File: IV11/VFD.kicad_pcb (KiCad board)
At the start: 2 copper layers, 225 x 80 mm, 72 parts, among them J1 USB_B, SW1 switch, SW2 switch, SW3 switch, SW4 switch, U1 74HC595, U10 UDN2981, U11 UDN2981, U12 UDN2981, U13 WeMos_mini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

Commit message: Remove OSHW logo - unfortunately with the generic modules, we can't meet OSHW requirements
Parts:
- removed the REF** at (55.4, 26.3)

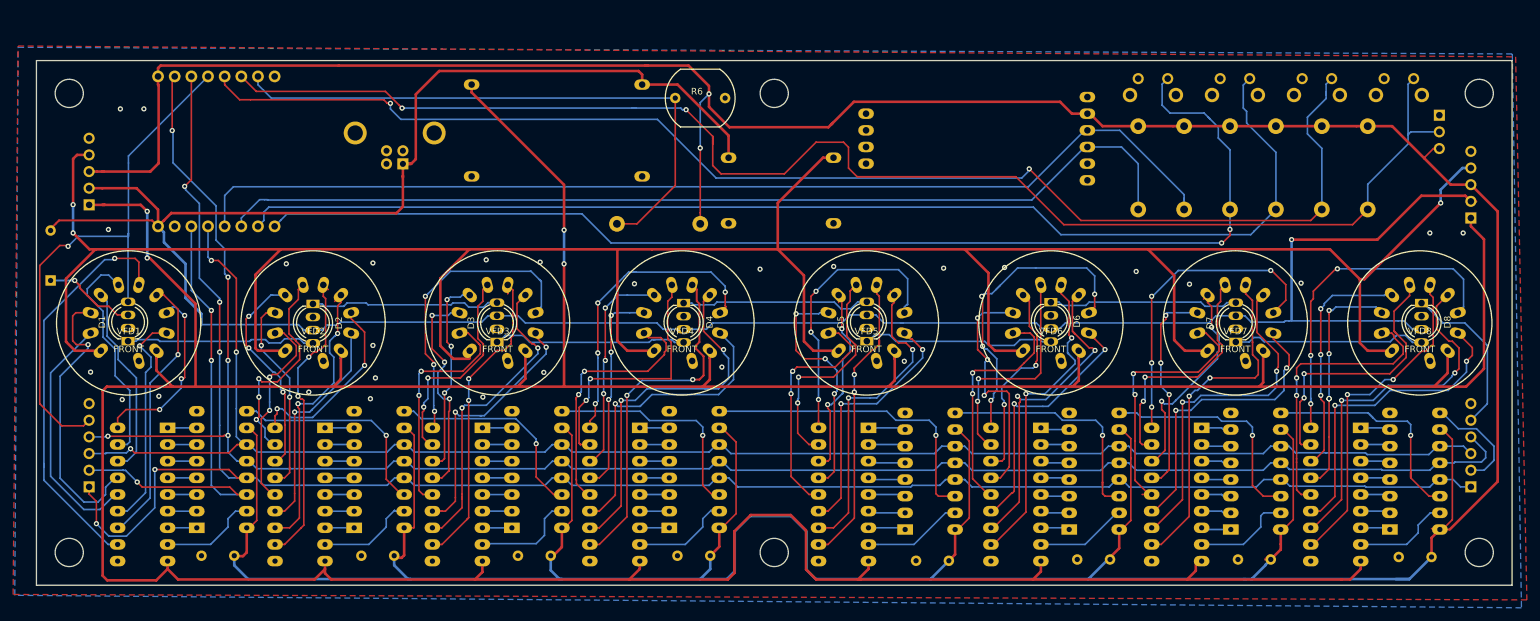
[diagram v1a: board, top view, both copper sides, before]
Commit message: Final updates to complete PCB revision 1.2 including an I2C breakout connector
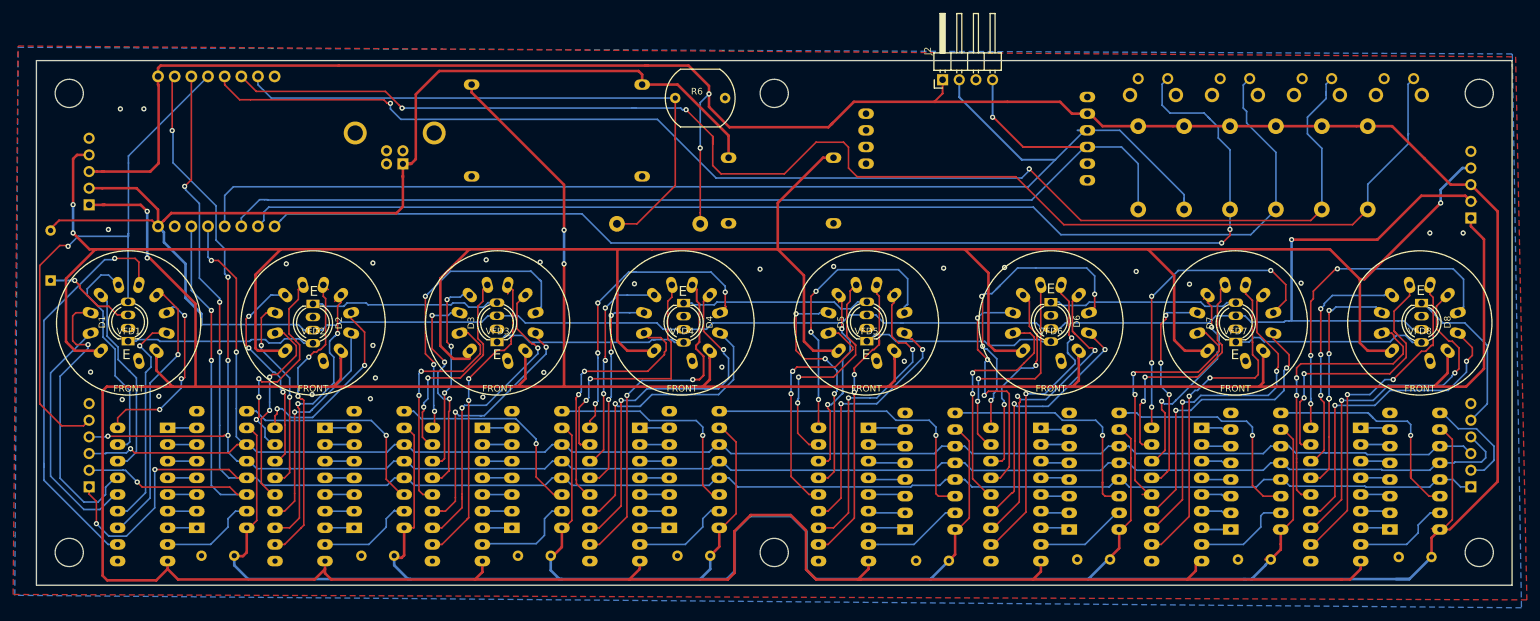
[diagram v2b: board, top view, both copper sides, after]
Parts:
- removed DS18B20: DS18B20, Connector_PinHeader_2.54mm:PinHeader_1x03_P2.54mm_Vertical
- added J2: I2C_CONN, Connector_PinHeader_2.54mm:PinHeader_1x04_P2.54mm_Horizontal, F.Cu at (138.2, 2.92)
- R5: value 100k -> 22k
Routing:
- net SCL: track 150.6 -> 174.2 mm, vias 0 -> 1
- net SDA: track 161.3 -> 184.1 mm
- net SW_1: track 220.2 -> 215.4 mm
- net +3V3: track 733.6 -> 735.1 mm
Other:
- board text added: "E"

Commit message: Major redesign to use different buck converter, and also up-rate track thickness for power rails
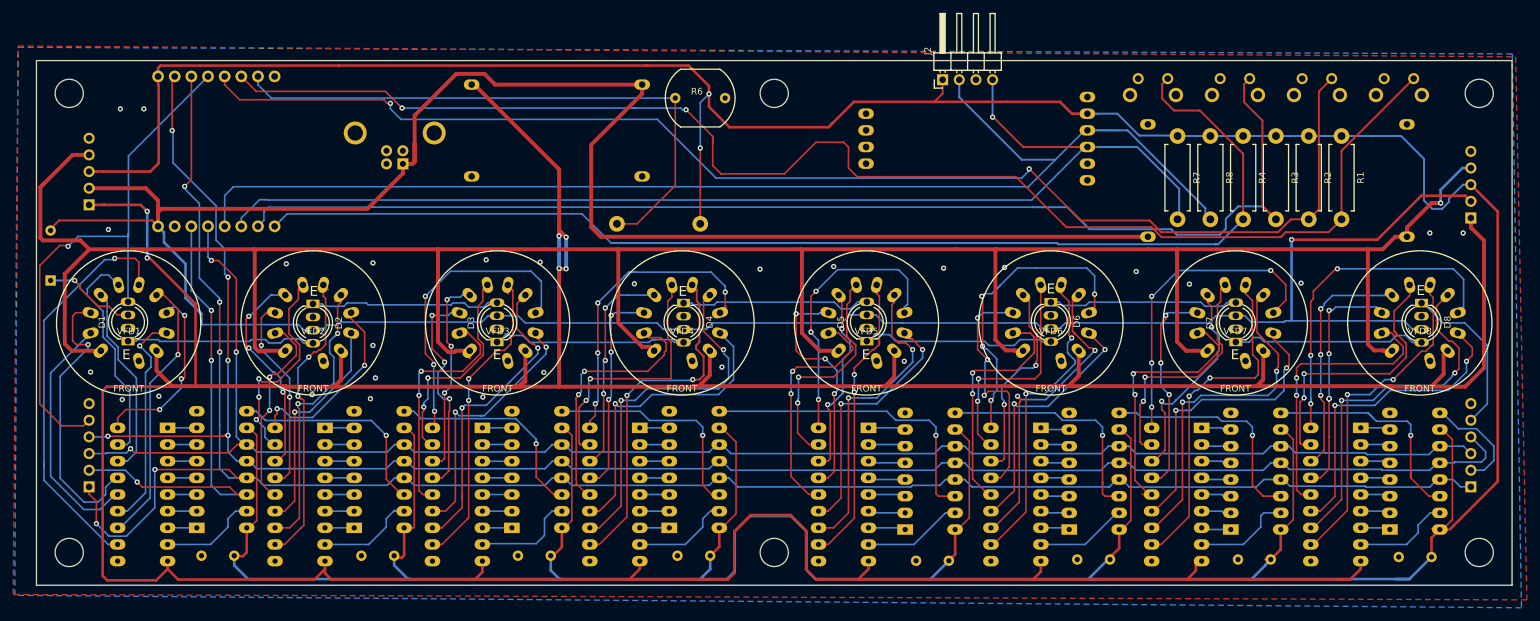
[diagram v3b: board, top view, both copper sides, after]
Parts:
- R1, R2, R3, R4, R7, R8: moved to F.Cu
- U18: value MiniBuckBoard -> LM2596BuckConverterModule; footprint GenericModules:MP2307BuckConverterModule -> GenericModules:LM2596BuckConverterModule
- moved U18 75.7 mm to (189.2, 18.3), turned to 0 degrees
- moved R7 6.18 mm to (174.0, 11.5)
- moved R1 4.27 mm to (199.0, 11.5)
- moved R8 4.27 mm to (179.0, 11.5)
- moved R2 2.50 mm to (194.0, 11.5)
- moved R4 2.50 mm to (184.0, 11.5)
- moved R3 1.50 mm to (189.0, 11.5)
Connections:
- U18 pad 1: +1V5 -> +5V
- U18 pad 4: +5V -> +1V5
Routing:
- net +36V: track 637.5 -> 748.7 mm, vias 4 -> 6
- net +5V: track 402.5 -> 488.4 mm
- net +1V5: track 422.7 -> 403.2 mm, vias 3 -> 1
- net SCL: track 174.2 -> 183.2 mm
- net +3V3: track 735.1 -> 741.9 mm
- net SDA: track 184.1 -> 190.7 mm
- net SW_3: track 182.9 -> 186.3 mm
- net SW_4: track 180.8 -> 181.4 mm, vias 2 -> 0
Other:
- board text added: "V1.3"
- board text removed: "1"
- board text removed: "2"
- board text removed: "3"
- board text removed: "V1.2"

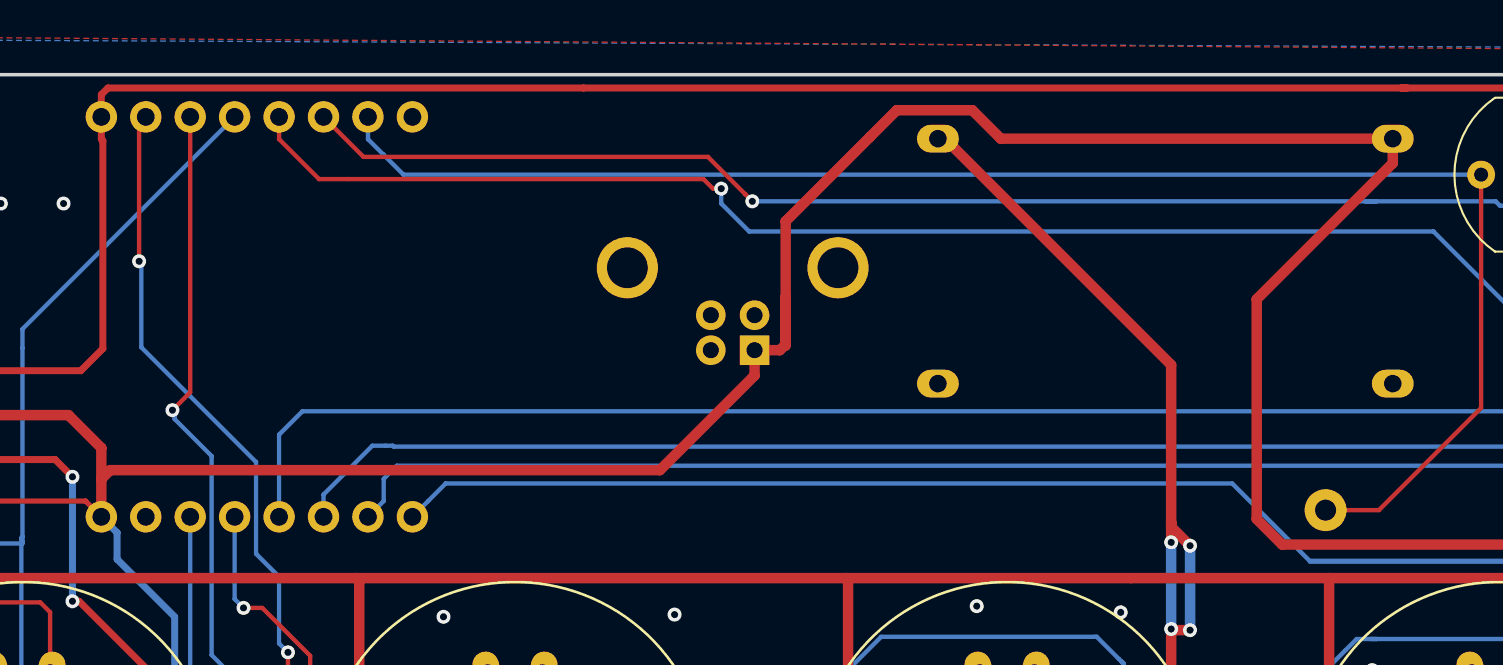
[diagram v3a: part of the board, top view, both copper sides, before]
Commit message: Add in room for polyfuse
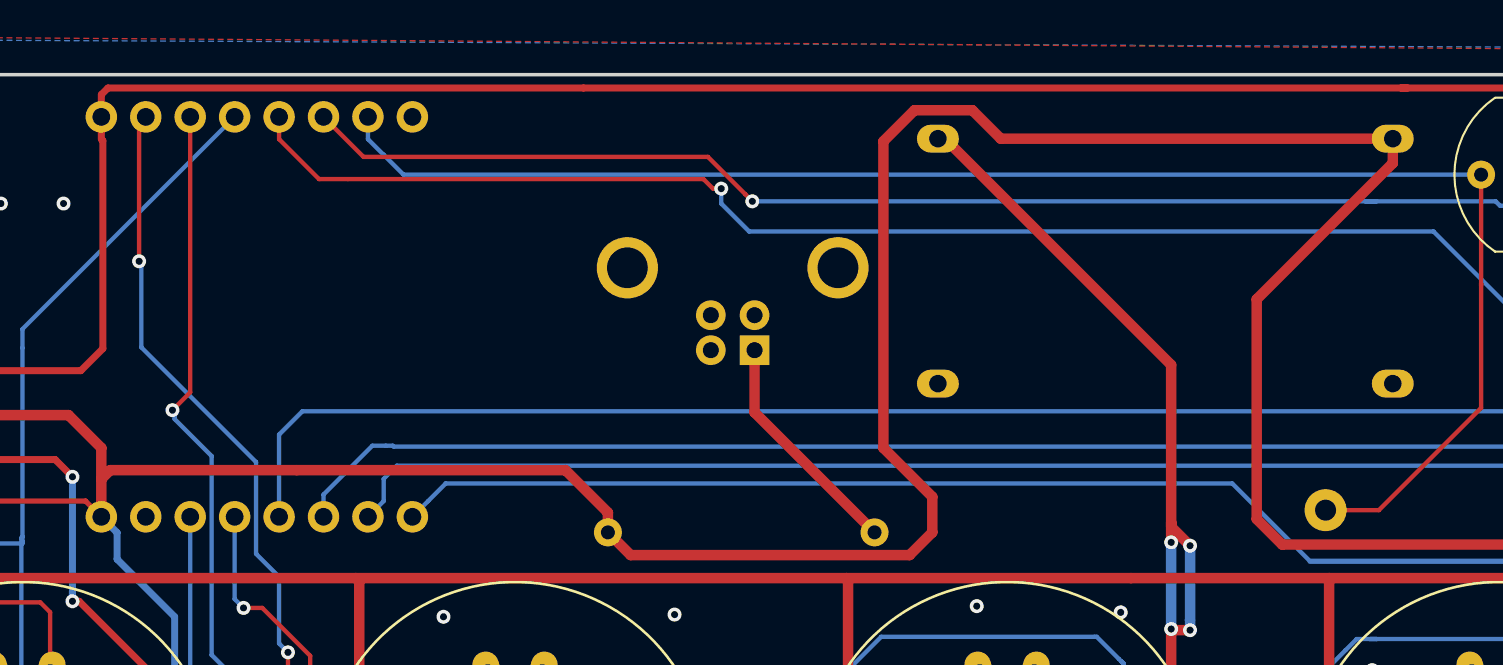
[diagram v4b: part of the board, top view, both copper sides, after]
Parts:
- added F1: Polyfuse, Resistor_THT:R_Axial_DIN0309_L9.0mm_D3.2mm_P15.24mm_Horizontal, B.Cu at (47.5, 26.2)
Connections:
- J1 pad 1: +5V -> Net-(F1-Pad2)
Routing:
- net +5V: track 488.4 -> 502.4 mm
- net Net-(F1-Pad2): track 0.00 -> 13.3 mm
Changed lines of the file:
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@@
     (thickness 1.6)
     (drawings 15)
-    (tracks 2302)
+    (tracks 2305)
     (zones 0)
-    (modules 71)
-    (nets 171)
+    (modules 72)
+    (nets 172)
   )
   (page A4)
@@
   )
   (setup
-    (last_trace_width 0.25)
+    (last_trace_width 0.6)
     (user_trace_width 0.3)
     (user_trace_width 0.4)
@@
   (net 169 "Net-(D6-Pad1)")
   (net 170 "Net-(D7-Pad1)")
+  (net 171 "Net-(F1-Pad2)")
   (net_class Default "This is the default net class."
     (clearance 0.2)
@@
     (add_net "Net-(D6-Pad1)")
     (add_net "Net-(D7-Pad1)")
+    (add_net "Net-(F1-Pad2)")
     (add_net "Net-(J1-Pad2)")
     (add_net "Net-(J1-Pad3)")
@@
       (net 148 "Net-(J1-Pad2)"))
     (pad 1 thru_hole rect (at 0 0 90) (size 1.7 1.7) (drill 0.92) (layers *.Cu *.Mask)
-      (net 147 +5V))
+      (net 171 "Net-(F1-Pad2)"))
     (model ${KISYS3DMOD}/Connector_USB.3dshapes/USB_B_OST_USB-B1HSxx_Horizontal.wrl
       (at (xyz 0 0 0))
@@
     )
   )
+  (module Resistor_THT:R_Axial_DIN0309_L9.0mm_D3.2mm_P15.24mm_Horizontal (layer B.Cu)
+    (at 47.498 26.162)
+    (descr "Resistor, Axial_DIN0309 series, Axial, Horizontal, pin pitch=15.24mm, 0.5W = 1/2W, length*diameter=9*3.2mm^2, http://cdn-reichelt.de/documents/datenblatt/B400/1_4W%23YAG.pdf")
+    (tags "Resistor Axial_DIN0309 series Axial Horizontal pin pitch 15.24mm 0.5W = 1/2W length 9mm diameter 3.2mm")
+    (fp_text reference F1 (at 7.62 2.72) (layer B.SilkS)
+      (effects (font (size 1 1) (thickness 0.15)) (justify mirror))
+    )
+    (fp_text value Polyfuse (at 7.62 -2.72) (layer B.Fab)
+      (effects (font (size 1 1) (thickness 0.15)) (justify mirror))
+    )
+    (fp_line (start 3.12 1.6) (end 3.12 -1.6) (layer B.Fab) (width 0.1))
+    (fp_line (start 3.12 -1.6) (end 12.12 -1.6) (layer B.Fab) (width 0.1))
+    (fp_line (start 12.12 -1.6) (end 12.12 1.6) (layer B.Fab) (width 0.1))
+    (fp_line (start 12.12 1.6) (end 3.12 1.6) (layer B.Fab) (width 0.1))
+    (fp_line (start 0 0) (end 3.12 0) (layer B.Fab) (width 0.1))
+    (fp_line (start 15.24 0) (end 12.12 0) (layer B.Fab) (width 0.1))
+    (fp_line (start 3 1.72) (end 3 -1.72) (layer B.SilkS) (width 0.12))
+    (fp_line (start 3 -1.72) (end 12.24 -1.72) (layer B.SilkS) (width 0.12))
+    (fp_line (start 12.24 -1.72) (end 12.24 1.72) (layer B.SilkS) (width 0.12))
+    (fp_line (start 12.24 1.72) (end 3 1.72) (layer B.SilkS) (width 0.12))
+    (fp_line (start 1.04 0) (end 3 0) (layer B.SilkS) (width 0.12))
+    (fp_line (start 14.2 0) (end 12.24 0) (layer B.SilkS) (width 0.12))
+    (fp_line (start -1.05 1.85) (end -1.05 -1.85) (layer B.CrtYd) (width 0.05))
+    (fp_line (start -1.05 -1.85) (end 16.29 -1.85) (layer B.CrtYd) (width 0.05))
+    (fp_line (start 16.29 -1.85) (end 16.29 1.85) (layer B.CrtYd) (width 0.05))
+    (fp_line (start 16.29 1.85) (end -1.05 1.85) (layer B.CrtYd) (width 0.05))
+    (fp_text user %R (at 7.62 0) (layer B.Fab)
+      (effects (font (size 1 1) (thickness 0.15)) (justify mirror))
+    )
+    (pad 1 thru_hole circle (at 0 0) (size 1.6 1.6) (drill 0.8) (layers *.Cu *.Mask)
+      (net 147 +5V))
+    (pad 2 thru_hole oval (at 15.24 0) (size 1.6 1.6) (drill 0.8) (layers *.Cu *.Mask)
+      (net 171 "Net-(F1-Pad2)"))
+    (model ${KISYS3DMOD}/Resistor_THT.3dshapes/R_Axial_DIN0309_L9.0mm_D3.2mm_P15.24mm_Horizontal.wrl
+      (at (xyz 0 0 0))
+      (scale (xyz 1 1 1))
+      (rotate (xyz 0 0 0))
+    )
+  )
   (gr_text E (at 211.074 35.052) (layer F.SilkS)
     (effects (font (size 1.5 1.5) (thickness 0.3)))
@@
   (segment (start 8.033 19.46) (end 16.666 19.46) (width 0.6) (layer F.Cu) (net 147))
   (segment (start 16.666 19.46) (end 18.542 21.336) (width 0.6) (layer F.Cu) (net 147))
-  (segment (start 55.88 17.198) (end 50.472 22.606) (width 0.6) (layer F.Cu) (net 147))
-  (segment (start 55.88 15.748) (end 55.88 17.198) (width 0.6) (layer F.Cu) (net 147))
   (segment (start 19.05 22.606) (end 18.542 23.114) (width 0.6) (layer F.Cu) (net 147))
-  (segment (start 50.472 22.606) (end 19.05 22.606) (width 0.6) (layer F.Cu) (net 147))
   (segment (start 18.542 21.336) (end 18.542 23.114) (width 0.6) (layer F.Cu) (net 147))
   (segment (start 18.542 23.114) (end 18.542 25.273) (width 0.6) (layer F.Cu) (net 147))
-  (segment (start 64.008 2.032) (end 62.484 3.556) (width 0.6) (layer F.Cu) (net 147))
-  (segment (start 68.326 2.032) (end 64.008 2.032) (width 0.6) (layer F.Cu) (net 147))
-  (segment (start 92.361 3.659) (end 69.953 3.659) (width 0.6) (layer F.Cu) (net 147))
-  (segment (start 62.484 3.556) (end 57.658 8.382) (width 0.6) (layer F.Cu) (net 147))
-  (segment (start 69.953 3.659) (end 68.326 2.032) (width 0.6) (layer F.Cu) (net 147))
-  (segment (start 57.658 15.42) (end 57.658 12.7) (width 0.6) (layer F.Cu) (net 147))
-  (segment (start 57.33 15.748) (end 57.658 15.42) (width 0.6) (layer F.Cu) (net 147))
-  (segment (start 57.658 8.382) (end 57.658 12.7) (width 0.6) (layer F.Cu) (net 147))
-  (segment (start 55.88 15.748) (end 57.33 15.748) (width 0.6) (layer F.Cu) (net 147))
-  (segment (start 57.658 12.7) (end 57.658 15.494) (width 0.6) (layer F.Cu) (net 147))
   (segment (start 169.48 26.858) (end 86.04 26.858) (width 0.6) (layer F.Cu) (net 147))
   (segment (start 86.04 26.858) (end 84.582 25.4) (width 0.6) (layer F.Cu) (net 147))
@@
   (segment (start 84.582 12.838) (end 92.361 5.059) (width 0.6) (layer F.Cu) (net 147))
   (segment (start 84.582 25.4) (end 84.582 12.838) (width 0.6) (layer F.Cu) (net 147))
+  (segment (start 45.07337 22.606) (end 29.718 22.606) (width 0.6) (layer F.Cu) (net 147))
+  (segment (start 47.498 25.03063) (end 45.07337 22.606) (width 0.6) (layer F.Cu) (net 147))
+  (segment (start 47.498 26.162) (end 47.498 25.03063) (width 0.6) (layer F.Cu) (net 147))
+  (segment (start 29.718 22.606) (end 19.05 22.606) (width 0.6) (layer F.Cu) (net 147))
+  (segment (start 48.798001 27.462001) (end 64.739999 27.462001) (width 0.6) (layer F.Cu) (net 147))
+  (segment (start 66.04 26.162) (end 66.04 24.13) (width 0.6) (layer F.Cu) (net 147))
+  (segment (start 47.498 26.162) (end 48.798001 27.462001) (width 0.6) (layer F.Cu) (net 147))
+  (segment (start 69.953 3.659) (end 92.361 3.659) (width 0.6) (layer F.Cu) (net 147))
+  (segment (start 68.326 2.032) (end 69.953 3.659) (width 0.6) (layer F.Cu) (net 147))
+  (segment (start 64.739999 27.462001) (end 66.04 26.162) (width 0.6) (layer F.Cu) (net 147))
+  (segment (start 63.246 3.81) (end 65.024 2.032) (width 0.6) (layer F.Cu) (net 147))
+  (segment (start 66.04 24.13) (end 63.246 21.336) (width 0.6) (layer F.Cu) (net 147))
+  (segment (start 63.246 21.336) (end 63.246 3.81) (width 0.6) (layer F.Cu) (net 147))
+  (segment (start 65.024 2.032) (end 68.326 2.032) (width 0.6) (layer F.Cu) (net 147))
   (segment (start 55.67787 75.819) (end 56.0705 75.42637) (width 0.4) (layer F.Cu) (net 150))
   (segment (start 54.5465 75.819) (end 55.67787 75.819) (width 0.4) (layer F.Cu) (net 150))
@@
   (segment (start 185.6105 42.2275) (end 186.577265 42.2275) (width 0.25) (layer B.Cu) (net 170))
   (segment (start 184.928 42.91) (end 185.6105 42.2275) (width 0.25) (layer B.Cu) (net 170))
+  (segment (start 55.88 19.304) (end 62.738 26.162) (width 0.6) (layer F.Cu) (net 171))
+  (segment (start 55.88 15.748) (end 55.88 19.304) (width 0.6) (layer F.Cu) (net 171))
   (zone (net 1) (net_name GND) (layer F.Cu) (hatch edge 0.508)
     (connect_pads (clearance 0.508))
